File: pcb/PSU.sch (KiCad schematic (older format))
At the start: 18 parts, among them Q3 DMG2305UX, Q4 BCM857BS, U18 NCP177, U9 AP7361C-33-FGE

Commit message: protection circuit added
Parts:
- removed U18: NCP177, SMD:DFN5B, symbol ncp177:NCP177
- added U18: TCR8BM12, SMD:DFN5B, symbol TCR8BM12:TCR8BM12
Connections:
- wire segments 71 -> 67
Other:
- moved on the sheet: C73
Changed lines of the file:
@@
 $EndDescr
 $Comp
-L power:+5V #PWR0108
+L power:+5V #PWR0107
 U 1 1 590B8A20
 P 3475 4775
-F 0 "#PWR0108" H 3475 4625 35  0001 C CNN
+F 0 "#PWR0107" H 3475 4625 35  0001 C CNN
 F 1 "+5V" H 3493 4949 35  0000 C CNN
 F 2 "" H 3475 4775 35  0000 C CNN
@@
 $EndComp
 $Comp
-L power:GND #PWR0109
+L power:GND #PWR0108
 U 1 1 590B8A68
 P 3475 5275
-F 0 "#PWR0109" H 3475 5025 35  0001 C CNN
+F 0 "#PWR0108" H 3475 5025 35  0001 C CNN
 F 1 "GND" H 3475 5195 35  0001 C CNN
 F 2 "" H 3475 5275 35  0000 C CNN
@@
 $EndComp
 $Comp
-L power:GND #PWR0110
+L power:GND #PWR0109
 U 1 1 590B8A6E
 P 2800 6075
-F 0 "#PWR0110" H 2800 5825 35  0001 C CNN
+F 0 "#PWR0109" H 2800 5825 35  0001 C CNN
 F 1 "GND" H 2808 5901 35  0000 C CNN
 F 2 "" H 2800 6075 35  0000 C CNN
@@
 $EndComp
 $Comp
-L power:GND #PWR0111
+L power:GND #PWR0110
 U 1 1 590B8A74
 P 3100 6075
-F 0 "#PWR0111" H 3100 5825 35  0001 C CNN
+F 0 "#PWR0110" H 3100 5825 35  0001 C CNN
 F 1 "GND" H 3108 5901 35  0000 C CNN
 F 2 "" H 3100 6075 35  0000 C CNN
@@
 Protection Circuit
 $Comp
-L power:+5V #PWR0112
+L power:+5V #PWR0111
 U 1 1 590BB025
 P 1750 1800
-F 0 "#PWR0112" H 1750 1650 35  0001 C CNN
+F 0 "#PWR0111" H 1750 1650 35  0001 C CNN
 F 1 "+5V" H 1750 1940 35  0000 C CNN
 F 2 "" H 1750 1800 60  0000 C CNN
@@
 $EndComp
 $Comp
-L power:GND #PWR0116
+L power:GND #PWR0112
 U 1 1 590BB032
 P 3575 2650
-F 0 "#PWR0116" H 3575 2650 30  0001 C CNN
+F 0 "#PWR0112" H 3575 2650 30  0001 C CNN
 F 1 "GND" H 3575 2580 30  0001 C CNN
 F 2 "" H 3575 2650 60  0000 C CNN
@@
 $EndComp
 $Comp
-L power:GND #PWR0117
+L power:GND #PWR0116
 U 1 1 590BB038
 P 1750 2450
-F 0 "#PWR0117" H 1750 2450 30  0001 C CNN
+F 0 "#PWR0116" H 1750 2450 30  0001 C CNN
 F 1 "GND" H 1750 2380 30  0001 C CNN
 F 2 "" H 1750 2450 60  0000 C CNN
@@
 $EndComp
 $Comp
-L power:GND #PWR0119
+L power:GND #PWR0117
 U 1 1 590BB04C
 P 2750 2650
-F 0 "#PWR0119" H 2750 2650 30  0001 C CNN
+F 0 "#PWR0117" H 2750 2650 30  0001 C CNN
 F 1 "GND" H 2750 2580 30  0001 C CNN
 F 2 "" H 2750 2650 60  0000 C CNN
@@
 $EndComp
 $Comp
-L power:GND #PWR0120
+L power:GND #PWR0119
 U 1 1 590BD61F
 P 2475 5250
-F 0 "#PWR0120" H 2475 5000 35  0001 C CNN
+F 0 "#PWR0119" H 2475 5000 35  0001 C CNN
 F 1 "GND" H 2483 5076 35  0000 C CNN
 F 2 "" H 2475 5250 35  0000 C CNN
@@
 	3150 4875 3200 4875
 $Comp
-L power:+5V #PWR0131
+L power:+5V #PWR0120
 U 1 1 590C658D
 P 4650 4600
-F 0 "#PWR0131" H 4650 4450 50  0001 C CNN
+F 0 "#PWR0120" H 4650 4450 50  0001 C CNN
 F 1 "+5V" H 4665 4773 50  0000 C CNN
 F 2 "" H 4650 4600 50  0001 C CNN
@@
 Connection ~ 4650 4650
 $Comp
-L power:GND #PWR0165
+L power:GND #PWR0131
 U 1 1 590C6A0A
 P 4650 5000
-F 0 "#PWR0165" H 4650 5000 30  0001 C CNN
+F 0 "#PWR0131" H 4650 5000 30  0001 C CNN
 F 1 "GND" H 4650 4930 30  0001 C CNN
 F 2 "" H 4650 5000 60  0000 C CNN
@@
 L Device:C C73
 U 1 1 5EA8621F
-P 5350 2125
-F 0 "C73" H 5465 2171 50  0000 L CNN
-F 1 "10u" H 5465 2080 50  0000 L CNN
-F 2 "Capacitor_SMD:C_0603_1608Metric" H 5388 1975 50  0001 C CNN
-F 3 "~" H 5350 2125 50  0001 C CNN
-F 4 "1276-6456-1-ND" H 5350 2125 50  0001 C CNN "DigiKey"
-	1    5350 2125
-	1    0    0    -1
-$EndComp
-Wire Wire Line
-	5350 1825 5350 1975
-Connection ~ 5350 1975
+P 5350 2175
+F 0 "C73" H 5465 2221 50  0000 L CNN
+F 1 "10u" H 5465 2130 50  0000 L CNN
+F 2 "Capacitor_SMD:C_0603_1608Metric" H 5388 2025 50  0001 C CNN
+F 3 "~" H 5350 2175 50  0001 C CNN
+F 4 "1276-6456-1-ND" H 5350 2175 50  0001 C CNN "DigiKey"
+	1    5350 2175
+	1    0    0    -1
+$EndComp
+Wire Wire Line
+	5350 1875 5350 2025
+Connection ~ 5350 2025
 Wire Wire Line
 	6750 2075 6750 2025
@@
 	7150 2025 6750 2025
 $Comp
+L power:GND #PWR0165
+U 1 1 5EA8622D
+P 5350 2325
+F 0 "#PWR0165" H 5350 2075 50  0001 C CNN
+F 1 "GND" H 5355 2152 50  0000 C CNN
+F 2 "" H 5350 2325 50  0001 C CNN
+F 3 "" H 5350 2325 50  0001 C CNN
+	1    5350 2325
+	1    0    0    -1
+$EndComp
+$Comp
 L power:GND #PWR0168
-U 1 1 5EA8622D
-P 5350 2275
-F 0 "#PWR0168" H 5350 2025 50  0001 C CNN
-F 1 "GND" H 5355 2102 50  0000 C CNN
-F 2 "" H 5350 2275 50  0001 C CNN
-F 3 "" H 5350 2275 50  0001 C CNN
-	1    5350 2275
-	1    0    0    -1
-$EndComp
-$Comp
-L power:GND #PWR0220
 U 1 1 5EA86233
 P 6750 2375
-F 0 "#PWR0220" H 6750 2125 50  0001 C CNN
+F 0 "#PWR0168" H 6750 2125 50  0001 C CNN
 F 1 "GND" H 6755 2202 50  0000 C CNN
 F 2 "" H 6750 2375 50  0001 C CNN
@@
 $EndComp
 $Comp
-L power:GND #PWR0221
+L power:GND #PWR0220
 U 1 1 5EA86239
 P 7150 2375
-F 0 "#PWR0221" H 7150 2125 50  0001 C CNN
+F 0 "#PWR0220" H 7150 2125 50  0001 C CNN
 F 1 "GND" H 7155 2202 50  0000 C CNN
 F 2 "" H 7150 2375 50  0001 C CNN
@@
 1.2V ice40 regulator\n
 $Comp
-L ventilator-PowerSymbols:1V2_ICE #PWR0222
+L ventilator-PowerSymbols:1V2_ICE #PWR0221
 U 1 1 5EA86240
 P 7800 2025
-F 0 "#PWR0222" H 7800 1985 30  0001 C CNN
+F 0 "#PWR0221" H 7800 1985 30  0001 C CNN
 F 1 "1V2_ICE" H 7809 2163 30  0000 C CNN
 F 2 "" H 7800 2025 60  0000 C CNN
@@
 	1    0    0    -1
 $EndComp
-$Comp
-L ncp177:NCP177 U18
-U 1 1 5EA86246
-P 6200 2175
-F 0 "U18" H 6200 2600 50  0000 C CNN
-F 1 "NCP177" H 6200 2509 50  0000 C CNN
-F 2 "SMD:DFN5B" H 5950 2475 50  0001 C CNN
-F 3 "" H 5950 2475 50  0001 C CNN
-	1    6200 2175
-	1    0    0    -1
-$EndComp
 Wire Wire Line
 	7150 2025 7800 2025
-Wire Wire Line
-	5350 1975 5675 1975
-Wire Wire Line
-	5675 2175 5675 1975
-Connection ~ 5675 1975
-Wire Wire Line
-	5675 1975 5800 1975
-Wire Wire Line
-	5675 2175 5800 2175
-$Comp
-L power:+3V3 #PWR0223
+$Comp
+L power:+3V3 #PWR0222
 U 1 1 5EA86252
-P 5350 1825
-F 0 "#PWR0223" H 5350 1675 50  0001 C CNN
-F 1 "+3V3" H 5365 1998 50  0000 C CNN
-F 2 "" H 5350 1825 50  0001 C CNN
-F 3 "" H 5350 1825 50  0001 C CNN
-	1    5350 1825
-	1    0    0    -1
-$EndComp
-$Comp
-L power:GND #PWR0224
+P 5350 1875
+F 0 "#PWR0222" H 5350 1725 50  0001 C CNN
+F 1 "+3V3" H 5365 2048 50  0000 C CNN
+F 2 "" H 5350 1875 50  0001 C CNN
+F 3 "" H 5350 1875 50  0001 C CNN
+	1    5350 1875
+	1    0    0    -1
+$EndComp
+$Comp
+L power:GND #PWR0223
 U 1 1 5EA86258
-P 6250 2575
-F 0 "#PWR0224" H 6250 2325 50  0001 C CNN
-F 1 "GND" H 6255 2402 50  0000 C CNN
-F 2 "" H 6250 2575 50  0001 C CNN
-F 3 "" H 6250 2575 50  0001 C CNN
-	1    6250 2575
-	1    0    0    -1
-$EndComp
-Wire Wire Line
-	6150 2525 6250 2525
-Wire Wire Line
-	6250 2525 6250 2575
-Connection ~ 6250 2525
-$Comp
-L power:+3V3 #PWR0225
+P 6200 2725
+F 0 "#PWR0223" H 6200 2475 50  0001 C CNN
+F 1 "GND" H 6205 2552 50  0000 C CNN
+F 2 "" H 6200 2725 50  0001 C CNN
+F 3 "" H 6200 2725 50  0001 C CNN
+	1    6200 2725
+	1    0    0    -1
+$EndComp
+Wire Wire Line
+	6200 2675 6200 2725
+$Comp
+L power:+3V3 #PWR0224
 U 1 1 5EA96191
 P 3575 1850
-F 0 "#PWR0225" H 3575 1700 50  0001 C CNN
+F 0 "#PWR0224" H 3575 1700 50  0001 C CNN
 F 1 "+3V3" H 3590 2023 50  0000 C CNN
 F 2 "" H 3575 1850 50  0001 C CNN
@@
 	1    0    0    -1
 $EndComp
+$Comp
+L TCR8BM12:TCR8BM12 U18
+U 1 1 5EA64067
+P 6250 2175
+F 0 "U18" H 6200 2590 50  0000 C CNB
+F 1 "TCR8BM12" H 6200 2499 50  0000 C CNN
+F 2 "SMD:DFN5B" H 6200 2175 50  0001 C CNN
+F 3 "" H 6200 2175 50  0001 C CNN
+	1    6250 2175
+	1    0    0    -1
+$EndComp
+Wire Wire Line
+	5350 2025 5800 2025
 $EndSCHEMATC

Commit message: mounting holes
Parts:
- F1: footprint ptc:PTC -> SMD:PTC
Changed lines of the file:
@@
 F 0 "F1" H 2250 4950 60  0000 C CNN
 F 1 "MF-MSMF250/X" H 2150 4800 35  0000 C CNN
-F 2 "ptc:PTC" H 2150 4875 60  0001 C CNN
+F 2 "SMD:PTC" H 2150 4875 60  0001 C CNN
 F 3 "" H 2150 4875 60  0001 C CNN
 	1    2150 4875

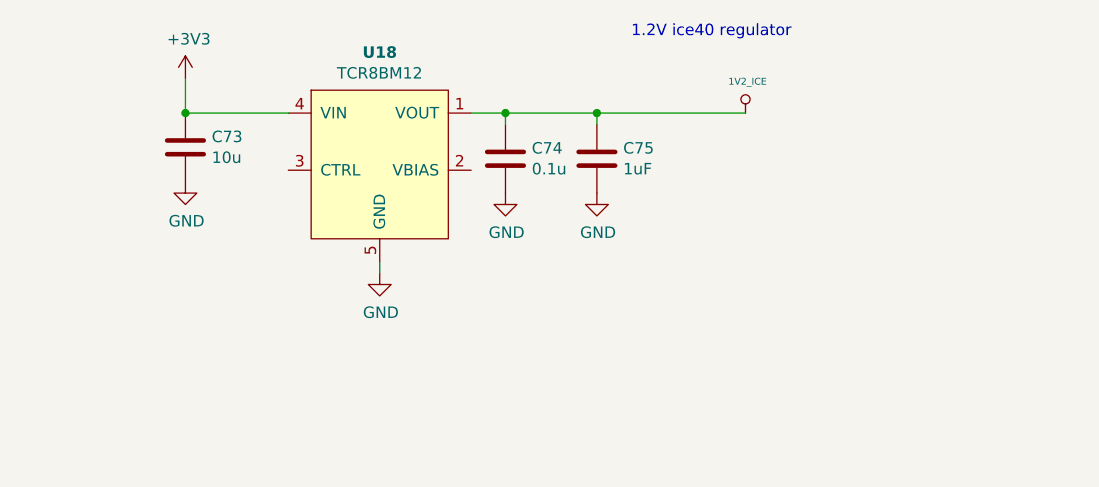
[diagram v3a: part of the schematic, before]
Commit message: new 1.2V DC-DC
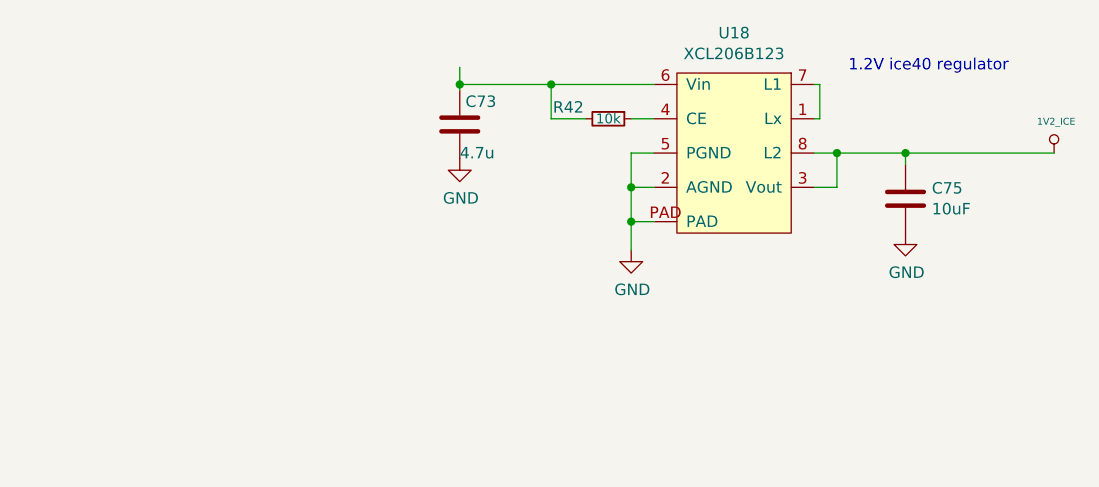
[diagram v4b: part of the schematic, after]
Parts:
- removed C74: 0.1u, Capacitor_SMD:C_0402_1005Metric, symbol Device:C
- removed U18: TCR8BM12, SMD:DFN5B, symbol TCR8BM12:TCR8BM12
- added R42: 10k, Resistor_SMD:R_0402_1005Metric, symbol Device:R_Small
- added U18: XCL206B123, SMD:CL-2025-02, symbol torex:XCL206
- C73: value 10u -> 4.7u
- C75: value 1uF -> 10uF
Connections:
- net +3V3: no longer C73.1
- net 1V2_ICE: now also U18.3 (Vout), U18.8 (L2)
- net GND: now also U18.2 (AGND), U18.5 (PGND), U18.PAD
- new net: C73.1, R42.2, U18.6 (Vin)
- new net: U18.1 (Lx), U18.7 (L1)
- new net: R42.1, U18.4 (CE)
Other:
- moved on the sheet: C73, C75
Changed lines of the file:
@@
 	4650 4950 4650 5000
-$Comp
-L Device:C C74
-U 1 1 5EA86211
-P 6750 2225
-F 0 "C74" H 6865 2271 50  0000 L CNN
-F 1 "0.1u" H 6865 2180 50  0000 L CNN
-F 2 "Capacitor_SMD:C_0402_1005Metric" H 6788 2075 50  0001 C CNN
-F 3 "~" H 6750 2225 50  0001 C CNN
-F 4 "720-1688-1-ND" H 6750 2225 50  0001 C CNN "DigiKey"
-	1    6750 2225
-	1    0    0    -1
-$EndComp
 $Comp
 L Device:C C75
 U 1 1 5EA86218
-P 7150 2225
-F 0 "C75" H 7265 2271 50  0000 L CNN
-F 1 "1uF" H 7265 2180 50  0000 L CNN
-F 2 "Capacitor_SMD:C_0603_1608Metric" H 7188 2075 50  0001 C CNN
-F 3 "~" H 7150 2225 50  0001 C CNN
-F 4 "445-14751-1-ND" H 7150 2225 50  0001 C CNN "DigiKey"
-	1    7150 2225
+P 8500 2400
+F 0 "C75" H 8615 2446 50  0000 L CNN
+F 1 "10uF" H 8615 2355 50  0000 L CNN
+F 2 "Capacitor_SMD:C_0603_1608Metric" H 8538 2250 50  0001 C CNN
+F 3 "~" H 8500 2400 50  0001 C CNN
+F 4 "445-14751-1-ND" H 8500 2400 50  0001 C CNN "DigiKey"
+	1    8500 2400
 	1    0    0    -1
 $EndComp
@@
 L Device:C C73
 U 1 1 5EA8621F
-P 5350 2175
-F 0 "C73" H 5465 2221 50  0000 L CNN
-F 1 "10u" H 5465 2130 50  0000 L CNN
-F 2 "Capacitor_SMD:C_0603_1608Metric" H 5388 2025 50  0001 C CNN
-F 3 "~" H 5350 2175 50  0001 C CNN
-F 4 "1276-6456-1-ND" H 5350 2175 50  0001 C CNN "DigiKey"
-	1    5350 2175
+P 6550 2075
+F 0 "C73" H 6575 2175 50  0000 L CNN
+F 1 "4.7u" H 6550 1950 50  0000 L CNN
+F 2 "Capacitor_SMD:C_0603_1608Metric" H 6588 1925 50  0001 C CNN
+F 3 "~" H 6550 2075 50  0001 C CNN
+F 4 "1276-6456-1-ND" H 6550 2075 50  0001 C CNN "DigiKey"
+	1    6550 2075
 	1    0    0    -1
 $EndComp
 Wire Wire Line
-	5350 1875 5350 2025
-Connection ~ 5350 2025
+	8500 2250 8500 2200
+Connection ~ 8500 2200
 Wire Wire Line
-	6750 2075 6750 2025
-Connection ~ 6750 2025
-Wire Wire Line
-	6750 2025 6600 2025
-Wire Wire Line
-	7150 2075 7150 2025
-Connection ~ 7150 2025
-Wire Wire Line
-	7150 2025 6750 2025
+	8500 2200 8200 2200
 $Comp
 L power:GND #PWR0165
 U 1 1 5EA8622D
-P 5350 2325
-F 0 "#PWR0165" H 5350 2075 50  0001 C CNN
-F 1 "GND" H 5355 2152 50  0000 C CNN
-F 2 "" H 5350 2325 50  0001 C CNN
-F 3 "" H 5350 2325 50  0001 C CNN
-	1    5350 2325
-	1    0    0    -1
-$EndComp
-$Comp
-L power:GND #PWR0168
-U 1 1 5EA86233
-P 6750 2375
-F 0 "#PWR0168" H 6750 2125 50  0001 C CNN
-F 1 "GND" H 6755 2202 50  0000 C CNN
-F 2 "" H 6750 2375 50  0001 C CNN
-F 3 "" H 6750 2375 50  0001 C CNN
-	1    6750 2375
+P 6550 2225
+F 0 "#PWR0165" H 6550 1975 50  0001 C CNN
+F 1 "GND" H 6555 2052 50  0000 C CNN
+F 2 "" H 6550 2225 50  0001 C CNN
+F 3 "" H 6550 2225 50  0001 C CNN
+	1    6550 2225
 	1    0    0    -1
 $EndComp
@@
 L power:GND #PWR0220
 U 1 1 5EA86239
-P 7150 2375
-F 0 "#PWR0220" H 7150 2125 50  0001 C CNN
-F 1 "GND" H 7155 2202 50  0000 C CNN
-F 2 "" H 7150 2375 50  0001 C CNN
-F 3 "" H 7150 2375 50  0001 C CNN
-	1    7150 2375
+P 8500 2550
+F 0 "#PWR0220" H 8500 2300 50  0001 C CNN
+F 1 "GND" H 8505 2377 50  0000 C CNN
+F 2 "" H 8500 2550 50  0001 C CNN
+F 3 "" H 8500 2550 50  0001 C CNN
+	1    8500 2550
 	1    0    0    -1
 $EndComp
-Text Notes 7300 1700 0    50   ~ 0
+Text Notes 8250 1850 0    50   ~ 0
 1.2V ice40 regulator\n
 $Comp
 L ventilator-PowerSymbols:1V2_ICE #PWR0221
 U 1 1 5EA86240
-P 7800 2025
-F 0 "#PWR0221" H 7800 1985 30  0001 C CNN
-F 1 "1V2_ICE" H 7809 2163 30  0000 C CNN
-F 2 "" H 7800 2025 60  0000 C CNN
-F 3 "" H 7800 2025 60  0000 C CNN
-	1    7800 2025
+P 9150 2200
+F 0 "#PWR0221" H 9150 2160 30  0001 C CNN
+F 1 "1V2_ICE" H 9159 2338 30  0000 C CNN
+F 2 "" H 9150 2200 60  0000 C CNN
+F 3 "" H 9150 2200 60  0000 C CNN
+	1    9150 2200
 	1    0    0    -1
 $EndComp
 Wire Wire Line
-	7150 2025 7800 2025
-$Comp
-L power:+3V3 #PWR0222
-U 1 1 5EA86252
-P 5350 1875
-F 0 "#PWR0222" H 5350 1725 50  0001 C CNN
-F 1 "+3V3" H 5365 2048 50  0000 C CNN
-F 2 "" H 5350 1875 50  0001 C CNN
-F 3 "" H 5350 1875 50  0001 C CNN
-	1    5350 1875
-	1    0    0    -1
-$EndComp
-$Comp
-L power:GND #PWR0223
-U 1 1 5EA86258
-P 6200 2725
-F 0 "#PWR0223" H 6200 2475 50  0001 C CNN
-F 1 "GND" H 6205 2552 50  0000 C CNN
-F 2 "" H 6200 2725 50  0001 C CNN
-F 3 "" H 6200 2725 50  0001 C CNN
-	1    6200 2725
-	1    0    0    -1
-$EndComp
-Wire Wire Line
-	6200 2675 6200 2725
+	8500 2200 9150 2200
 $Comp
 L power:+3V3 #PWR0224
@@
 $EndComp
 $Comp
-L TCR8BM12:TCR8BM12 U18
-U 1 1 5EA64067
-P 6250 2175
-F 0 "U18" H 6200 2590 50  0000 C CNB
-F 1 "TCR8BM12" H 6200 2499 50  0000 C CNN
-F 2 "SMD:DFN5B" H 6200 2175 50  0001 C CNN
-F 3 "" H 6200 2175 50  0001 C CNN
-	1    6250 2175
+L torex:XCL206 U18
+U 1 1 5ED6887F
+P 7750 2100
+F 0 "U18" H 7750 2525 50  0000 C CNN
+F 1 " XCL206B123" H 7750 2434 50  0000 C CNN
+F 2 "SMD:CL-2025-02" H 7850 2300 50  0001 C CNN
+F 3 "" H 7850 2300 50  0001 C CNN
+F 4 " 893-1404-6-ND " H 7750 2100 50  0001 C CNN "DigiKey"
+	1    7750 2100
+	-1   0    0    -1
+$EndComp
+Wire Wire Line
+	8100 2350 8200 2350
+Wire Wire Line
+	8200 2350 8200 2200
+Connection ~ 8200 2200
+Wire Wire Line
+	8200 2200 8100 2200
+Wire Wire Line
+	7400 2200 7300 2200
+Wire Wire Line
+	7300 2200 7300 2350
+Wire Wire Line
+	7400 2350 7300 2350
+Connection ~ 7300 2350
+Wire Wire Line
+	7300 2350 7300 2500
+Wire Wire Line
+	7400 2500 7300 2500
+Connection ~ 7300 2500
+Wire Wire Line
+	7300 2500 7300 2625
+$Comp
+L Device:R_Small R42
+U 1 1 5ED7F4CC
+P 7200 2050
+F 0 "R42" V 7150 1875 50  0000 C CNN
+F 1 "10k" V 7200 2050 43  0000 C CNN
+F 2 "Resistor_SMD:R_0402_1005Metric" H 7200 2050 50  0001 C CNN
+F 3 "~" H 7200 2050 50  0001 C CNN
+	1    7200 2050
+	0    1    1    0
+$EndComp
+$Comp
+L power:GND #PWR0168
+U 1 1 5ED87540
+P 7300 2625
+F 0 "#PWR0168" H 7300 2375 50  0001 C CNN
+F 1 "GND" H 7305 2452 50  0000 C CNN
+F 2 "" H 7300 2625 50  0001 C CNN
+F 3 "" H 7300 2625 50  0001 C CNN
+	1    7300 2625
 	1    0    0    -1
 $EndComp
 Wire Wire Line
-	5350 2025 5800 2025
+	8100 2050 8125 2050
+Wire Wire Line
+	8125 2050 8125 1900
+Wire Wire Line
+	8125 1900 8100 1900
+Wire Wire Line
+	7400 1900 6950 1900
+Wire Wire Line
+	6950 1900 6950 2050
+Wire Wire Line
+	6950 2050 7100 2050
+Wire Wire Line
+	7300 2050 7400 2050
+Wire Wire Line
+	6550 1825 6550 1900
+Wire Wire Line
+	6950 1900 6550 1900
+Connection ~ 6950 1900
+Connection ~ 6550 1900
+Wire Wire Line
+	6550 1900 6550 1925
 $EndSCHEMATC
